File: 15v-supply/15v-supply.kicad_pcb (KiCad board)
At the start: 2 copper layers, 127.5 x 101.9 mm, 0 parts

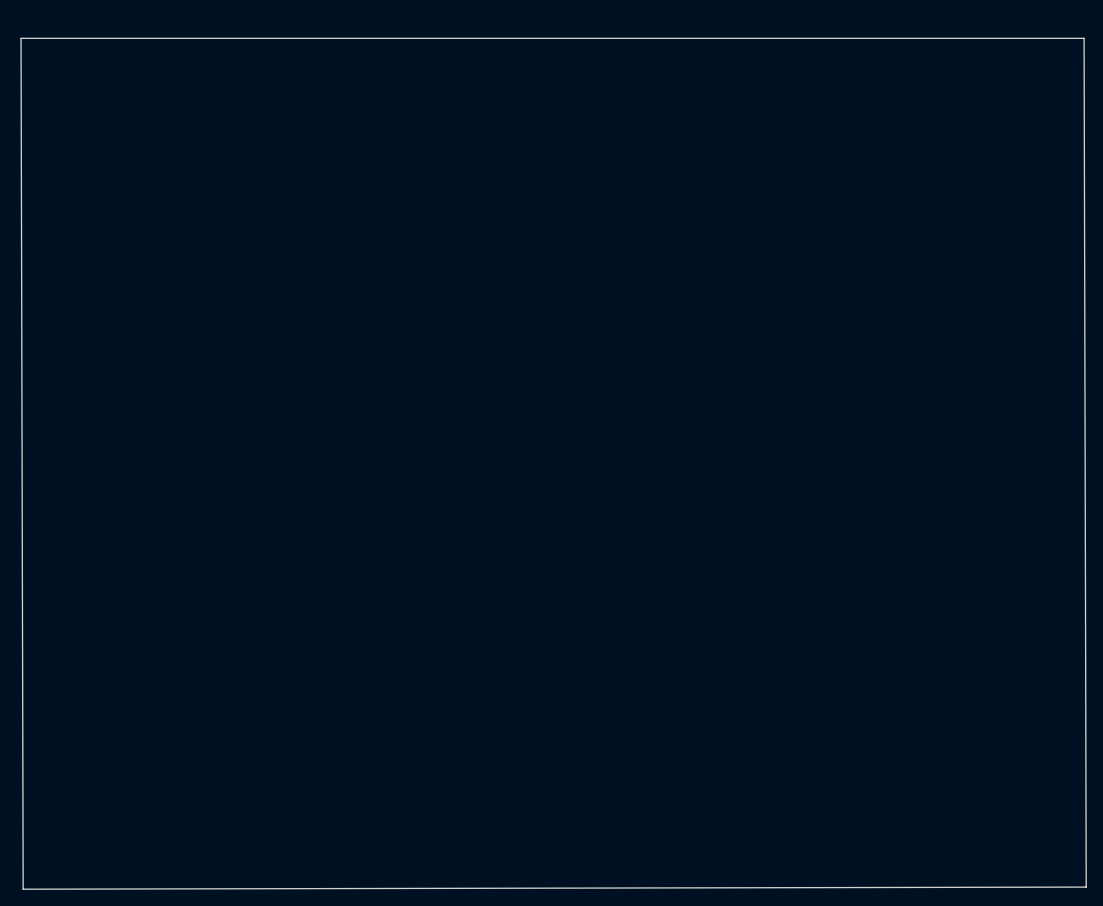
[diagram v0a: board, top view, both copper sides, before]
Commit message: 15v-supply routed and poured
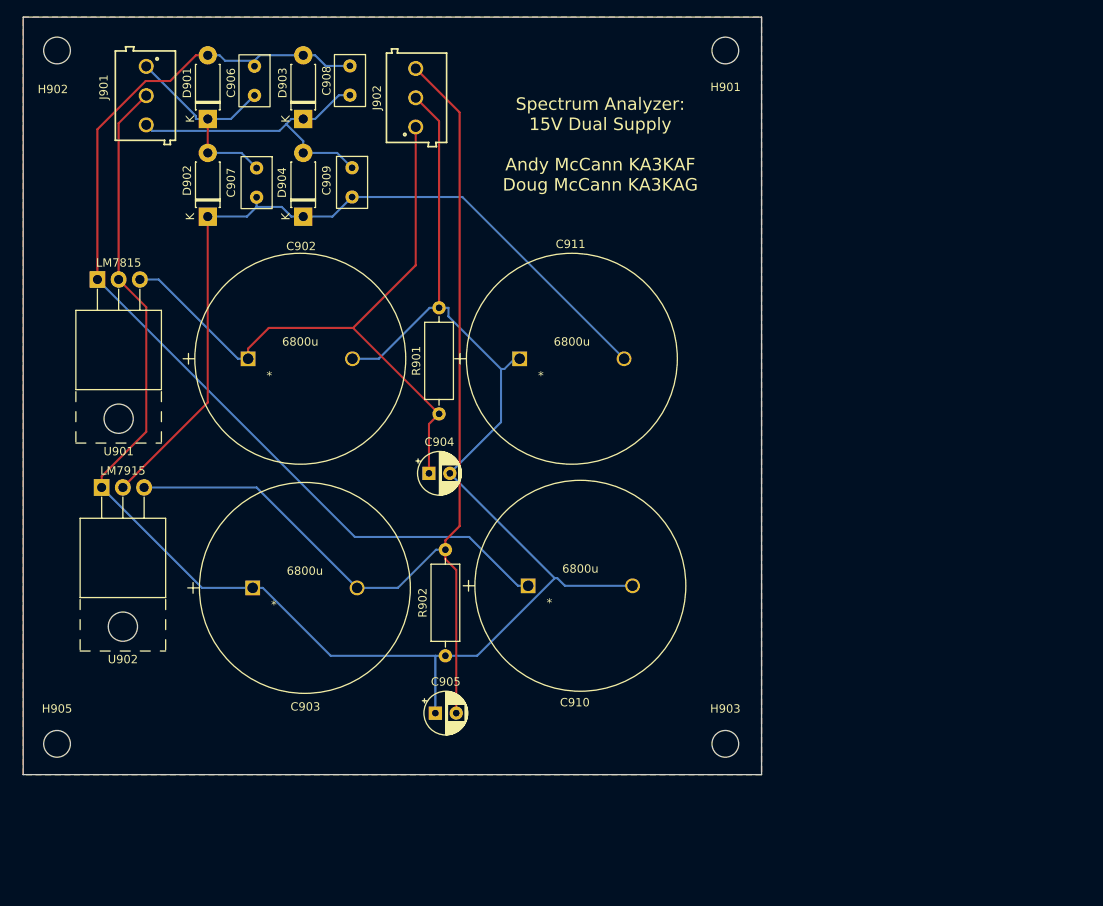
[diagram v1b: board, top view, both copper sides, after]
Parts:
- added C902: 6800u, 15v-supply:6800u-UVR1H682MRD6, F.Cu at (102.9, 88.9)
- added C903: 6800u, 15v-supply:6800u-UVR1H682MRD6, F.Cu at (103.4, 116.3)
- added C904: 6.8u, Capacitor_THT:CP_Radial_D5.0mm_P2.50mm, F.Cu at (124.5, 102.6)
- added C905: 6.8u, Capacitor_THT:CP_Radial_D5.0mm_P2.50mm, F.Cu at (125.3, 131.3)
- added C906: 0.01u, 15v-supply:C_Rect_L6.0mm_W3.5mm_P3.5mm_QYX1H103JTP3TA, F.Cu at (103.6, 53.9)
- added C907: 0.01u, 15v-supply:C_Rect_L6.0mm_W3.5mm_P3.5mm_QYX1H103JTP3TA, F.Cu at (103.9, 66.1)
- added C908: 0.01u, 15v-supply:C_Rect_L6.0mm_W3.5mm_P3.5mm_QYX1H103JTP3TA, F.Cu at (115.1, 53.8)
- added C909: 0.01u, 15v-supply:C_Rect_L6.0mm_W3.5mm_P3.5mm_QYX1H103JTP3TA, F.Cu at (115.3, 66.0)
- added C910: 6800u, 15v-supply:6800u-UVR1H682MRD6, F.Cu at (136.4, 116.1)
- added C911: 6800u, 15v-supply:6800u-UVR1H682MRD6, F.Cu at (135.4, 88.9)
- added D901: 1n5060, Diode_THT:D_DO-41_SOD81_P7.62mm_Horizontal, F.Cu at (98.0, 60.2)
- added D902: 1n5060, Diode_THT:D_DO-41_SOD81_P7.62mm_Horizontal, F.Cu at (98.0, 71.9)
- added D903: 1n5060, Diode_THT:D_DO-41_SOD81_P7.62mm_Horizontal, F.Cu at (109.5, 60.2)
- added D904: 1n5060, Diode_THT:D_DO-41_SOD81_P7.62mm_Horizontal, F.Cu at (109.5, 71.9)
- added H901: MountingHole, MountingHole:MountingHole_3.2mm_M3, F.Cu at (160.0, 52.0)
- added H902: MountingHole, MountingHole:MountingHole_3.2mm_M3, F.Cu at (80.0, 52.0)
- added H903: MountingHole, MountingHole:MountingHole_3.2mm_M3, F.Cu at (160.0, 135.0)
- added H905: MountingHole, MountingHole:MountingHole_3.2mm_M3, F.Cu at (80.0, 135.0)
- added J901: 691103110003, 15v-supply:terminal-block-691103110003, F.Cu at (90.7, 57.4)
- added J902: 691103110003, 15v-supply:terminal-block-691103110003, F.Cu at (122.9, 57.7)
- added R901: 2.2k, Resistor_THT:R_Axial_DIN0309_L9.0mm_D3.2mm_P12.70mm_Horizontal, F.Cu at (125.7, 95.5)
- added R902: 2.2k, Resistor_THT:R_Axial_DIN0309_L9.0mm_D3.2mm_P12.70mm_Horizontal, F.Cu at (126.5, 124.5)
- added U901: LM7815, Package_TO_SOT_THT:TO-220-3_Horizontal_TabUp, F.Cu at (84.8, 79.4)
- added U902: LM7915, Package_TO_SOT_THT:TO-220-3_Horizontal_TabUp, F.Cu at (85.3, 104.3)
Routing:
- net GND: track 0.00 -> 220.6 mm
- net /-15 REGULATED: track 0.00 -> 123.5 mm
- net /7815 IN: track 0.00 -> 120.3 mm
- net /7915 IN: track 0.00 -> 97.6 mm
- net /+15 REGULATED: track 0.00 -> 81.0 mm
- net /TRAN OUT2: track 0.00 -> 37.3 mm
- net /TRAN OUT1: track 0.00 -> 27.6 mm
- added copper zone on B.Cu, net GND
- added copper zone on F.Cu, net GND
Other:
- board size 127.5 x 101.9 mm -> 88.4 x 90.7 mm
- board text added: "Spectrum Analyzer: 15V Dual Supply Andy McCann KA3KAF Doug McCann KA3KAG"

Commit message: if and log amp routing and 3d model
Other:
- board text added: "Spectrum Analyzer: 15V Dual Supply Rev 0.0 Andy McCann KA3KAF Doug McCann KA3KAG"
- board text removed: "Spectrum Analyzer: 15V Dual Supply Andy McCann KA3KAF Doug McCann KA3KAG"
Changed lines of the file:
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@@
   )
   (gr_rect (start 75.946 48.006) (end 164.338 138.684) (layer "Edge.Cuts") (width 0.1) (fill none))
-  (gr_text "Spectrum Analyzer: \n15V Dual Supply\n\nAndy McCann KA3KAF\nDoug McCann KA3KAG" (at 145.034 63.246) (layer "F.SilkS")
-    (effects (font (size 1.5 1.5) (thickness 0.3)))
+  (gr_text "Spectrum Analyzer: \n15V Dual Supply \nRev 0.0\n\nAndy McCann KA3KAF\nDoug McCann KA3KAG" (at 131.826 62.484) (layer "F.SilkS")
+    (effects (font (size 1.5 1.5) (thickness 0.3)) (justify left))
   )
   (segment (start 124.5249 96.7091) (end 125.73 95.504) (width 0.25) (layer "F.Cu") (net 1))

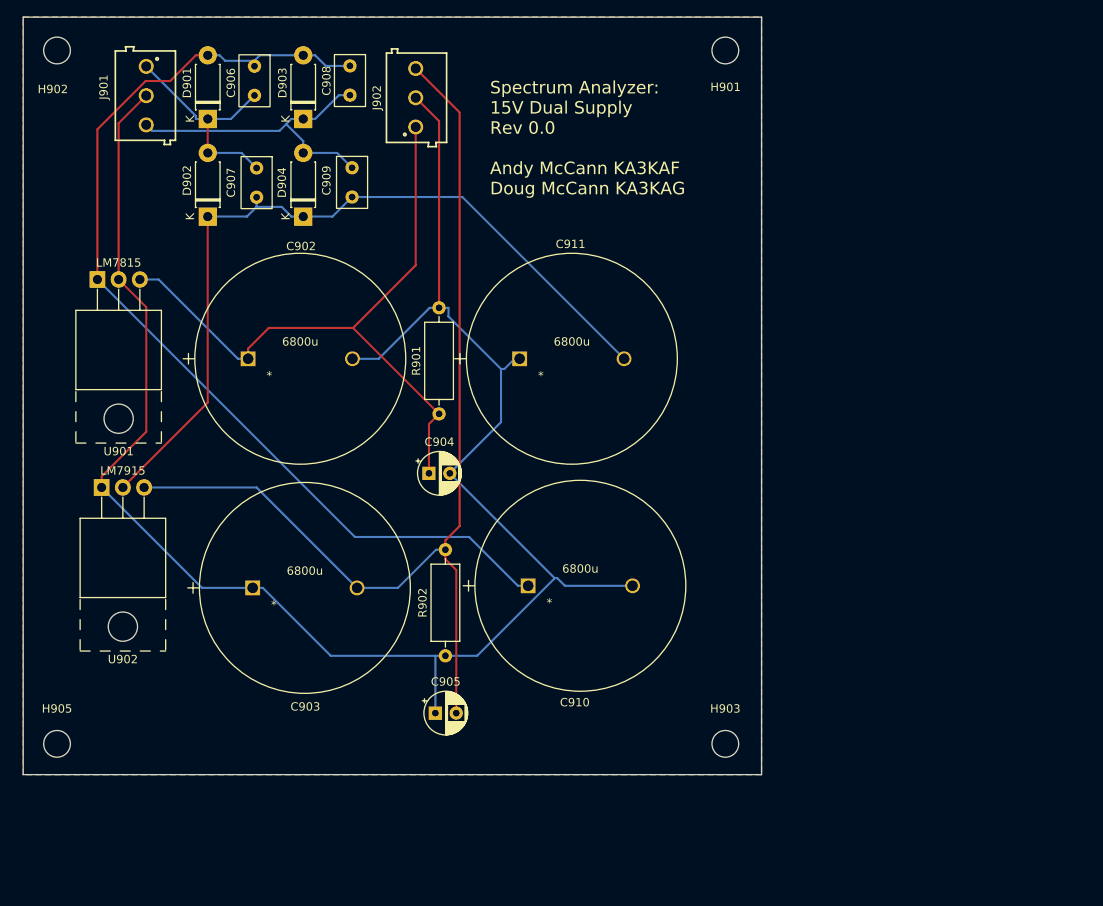
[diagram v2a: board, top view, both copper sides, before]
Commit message: updates to 15v supply and if and log amp boards so boards can be sent to fab
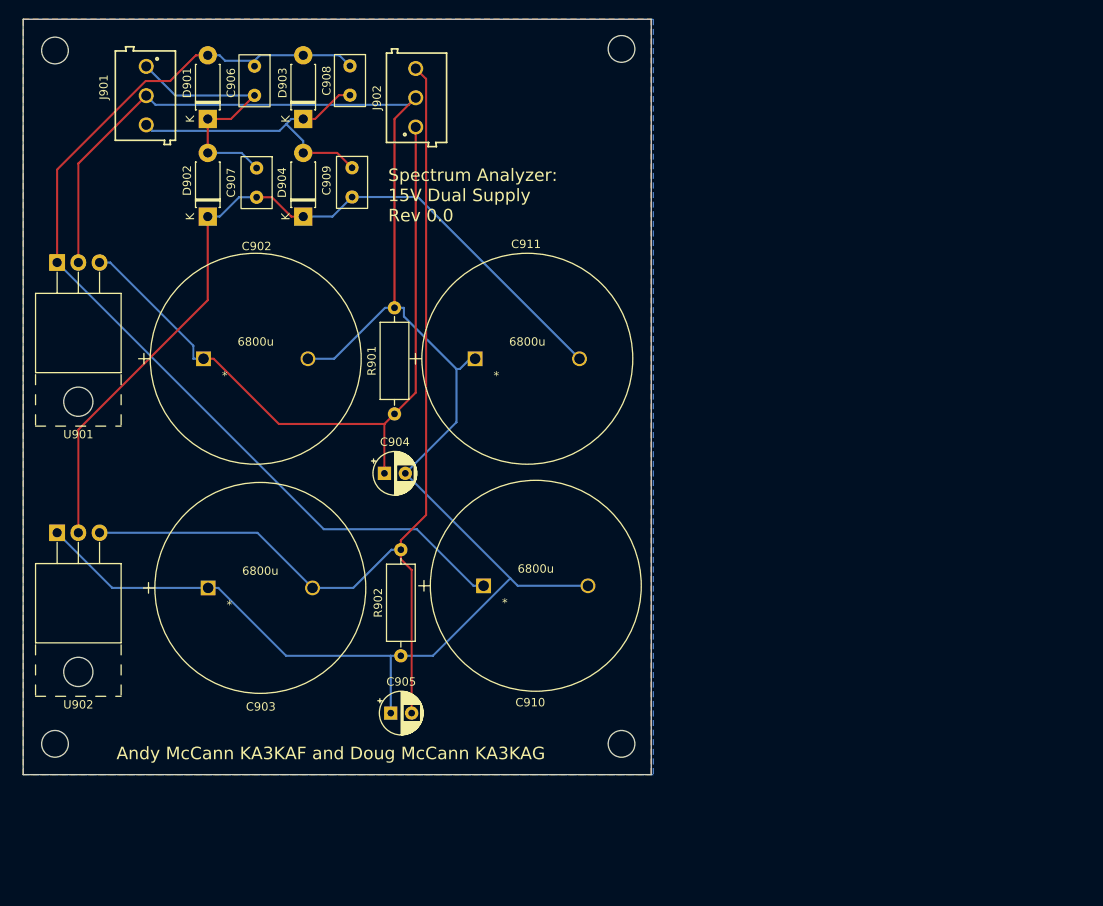
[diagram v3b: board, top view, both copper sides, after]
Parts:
- moved H901 12.4 mm to (147.6, 51.8)
- moved H903 12.4 mm to (147.6, 135.0)
- moved U902 7.60 mm to (80.0, 109.7)
- moved C902 5.33 mm to (97.5, 88.9)
- moved C904 5.33 mm to (119.2, 102.6)
- moved C905 5.33 mm to (120.0, 131.3)
- moved C910 5.33 mm to (131.1, 116.1)
- moved C911 5.33 mm to (130.0, 88.9)
- moved R901 5.33 mm to (120.4, 95.5)
- moved R902 5.33 mm to (121.2, 124.5)
- moved C903 5.33 mm to (98.1, 116.3)
- moved U901 5.24 mm to (80.0, 77.4)
- moved H902 0.24 mm to (79.8, 52.0)
- moved H905 0.24 mm to (79.8, 135.0)
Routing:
- net /+15 REGULATED: track 81.0 -> 86.0 mm
- net /TRAN OUT1: track 27.6 -> 31.8 mm
- net /-15 REGULATED: track 123.5 -> 120.2 mm
- net GND: track 220.6 -> 222.8 mm
- net /7915 IN: track 97.6 -> 99.7 mm
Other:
- board size 88.4 x 90.7 mm -> 75.2 x 90.4 mm
- board text added: "Andy McCann KA3KAF and Doug McCann KA3KAG"
- board text added: "Spectrum Analyzer: 15V Dual Supply Rev 0.0"
- board text removed: "Spectrum Analyzer: 15V Dual Supply Rev 0.0 Andy McCann KA3KAF Doug McCann KA3KAG"

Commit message: 15v-supply changes
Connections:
- D901 pad 1: /TRAN OUT1 -> /7815 IN
- D901 pad 2: /7815 IN -> /TRAN OUT1
- D902 pad 1: /7915 IN -> /TRAN OUT2
- D902 pad 2: /TRAN OUT1 -> /7915 IN
- D903 pad 1: /TRAN OUT2 -> /7815 IN
- D903 pad 2: /7815 IN -> /TRAN OUT2
- D904 pad 1: /7915 IN -> /TRAN OUT2
- D904 pad 2: /TRAN OUT2 -> /7915 IN
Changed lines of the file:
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@@
     (property "Spice_Model" "1N5060")
     (property "Spice_Netlist_Enabled" "Y")
+    (property "Spice_Node_Sequence" "2 1")
     (property "Spice_Primitive" "D")
     (attr through_hole)
@@
     (fp_line (start 7.62 0) (end 6.41 0) (layer "F.Fab") (width 0.1))
     (pad "1" thru_hole rect (at 0 0 90) (size 2.2 2.2) (drill 1.1) (layers *.Cu *.Mask)
-      (net 5 "/TRAN OUT1") (pinfunction "Cathode") (pintype "passive"))
+      (net 4 "/7815 IN") (pinfunction "Cathode") (pintype "passive"))
     (pad "2" thru_hole oval (at 7.62 0 90) (size 2.2 2.2) (drill 1.1) (layers *.Cu *.Mask)
-      (net 4 "/7815 IN") (pinfunction "Anode") (pintype "passive"))
+      (net 5 "/TRAN OUT1") (pinfunction "Anode") (pintype "passive"))
     (model "${KICAD6_3DMODEL_DIR}/Diode_THT.3dshapes/D_DO-41_SOD81_P7.62mm_Horizontal.wrl"
       (offset (xyz 0 0 0))
@@
     (property "Spice_Model" "1N5060")
     (property "Spice_Netlist_Enabled" "Y")
+    (property "Spice_Node_Sequence" "2 1")
     (property "Spice_Primitive" "D")
     (attr through_hole)
@@
     (fp_line (start 1.99 -1.35) (end 1.99 1.35) (layer "F.Fab") (width 0.1))
     (pad "1" thru_hole rect (at 0 0 90) (size 2.2 2.2) (drill 1.1) (layers *.Cu *.Mask)
-      (net 6 "/7915 IN") (pinfunction "Cathode") (pintype "passive"))
+      (net 7 "/TRAN OUT2") (pinfunction "Cathode") (pintype "passive"))
     (pad "2" thru_hole oval (at 7.62 0 90) (size 2.2 2.2) (drill 1.1) (layers *.Cu *.Mask)
-      (net 7 "/TRAN OUT2") (pinfunction "Anode") (pintype "passive"))
+      (net 6 "/7915 IN") (pinfunction "Anode") (pintype "passive"))
     (model "${KICAD6_3DMODEL_DIR}/Diode_THT.3dshapes/D_DO-41_SOD81_P7.62mm_Horizontal.wrl"
       (offset (xyz 0 0 0))
@@
     (property "Spice_Model" "1N5060")
     (property "Spice_Netlist_Enabled" "Y")
+    (property "Spice_Node_Sequence" "2 1")
     (property "Spice_Primitive" "D")
     (attr through_hole)
@@
     (fp_line (start 1.21 -1.35) (end 1.21 1.35) (layer "F.Fab") (width 0.1))
     (pad "1" thru_hole rect (at 0 0 90) (size 2.2 2.2) (drill 1.1) (layers *.Cu *.Mask)
-      (net 6 "/7915 IN") (pinfunction "Cathode") (pintype "passive"))
+      (net 7 "/TRAN OUT2") (pinfunction "Cathode") (pintype "passive"))
     (pad "2" thru_hole oval (at 7.62 0 90) (size 2.2 2.2) (drill 1.1) (layers *.Cu *.Mask)
-      (net 5 "/TRAN OUT1") (pinfunction "Anode") (pintype "passive"))
+      (net 6 "/7915 IN") (pinfunction "Anode") (pintype "passive"))
     (model "${KICAD6_3DMODEL_DIR}/Diode_THT.3dshapes/D_DO-41_SOD81_P7.62mm_Horizontal.wrl"
       (offset (xyz 0 0 0))
@@
     (property "Spice_Model" "1N5060")
     (property "Spice_Netlist_Enabled" "Y")
+    (property "Spice_Node_Sequence" "2 1")
     (property "Spice_Primitive" "D")
     (attr through_hole)
@@
     (fp_line (start 1.89 -1.35) (end 1.89 1.35) (layer "F.Fab") (width 0.1))
     (pad "1" thru_hole rect (at 0 0 90) (size 2.2 2.2) (drill 1.1) (layers *.Cu *.Mask)
-      (net 7 "/TRAN OUT2") (pinfunction "Cathode") (pintype "passive"))
+      (net 4 "/7815 IN") (pinfunction "Cathode") (pintype "passive"))
     (pad "2" thru_hole oval (at 7.62 0 90) (size 2.2 2.2) (drill 1.1) (layers *.Cu *.Mask)
-      (net 4 "/7815 IN") (pinfunction "Anode") (pintype "passive"))
+      (net 7 "/TRAN OUT2") (pinfunction "Anode") (pintype "passive"))
     (model "${KICAD6_3DMODEL_DIR}/Diode_THT.3dshapes/D_DO-41_SOD81_P7.62mm_Horizontal.wrl"
       (offset (xyz 0 0 0))

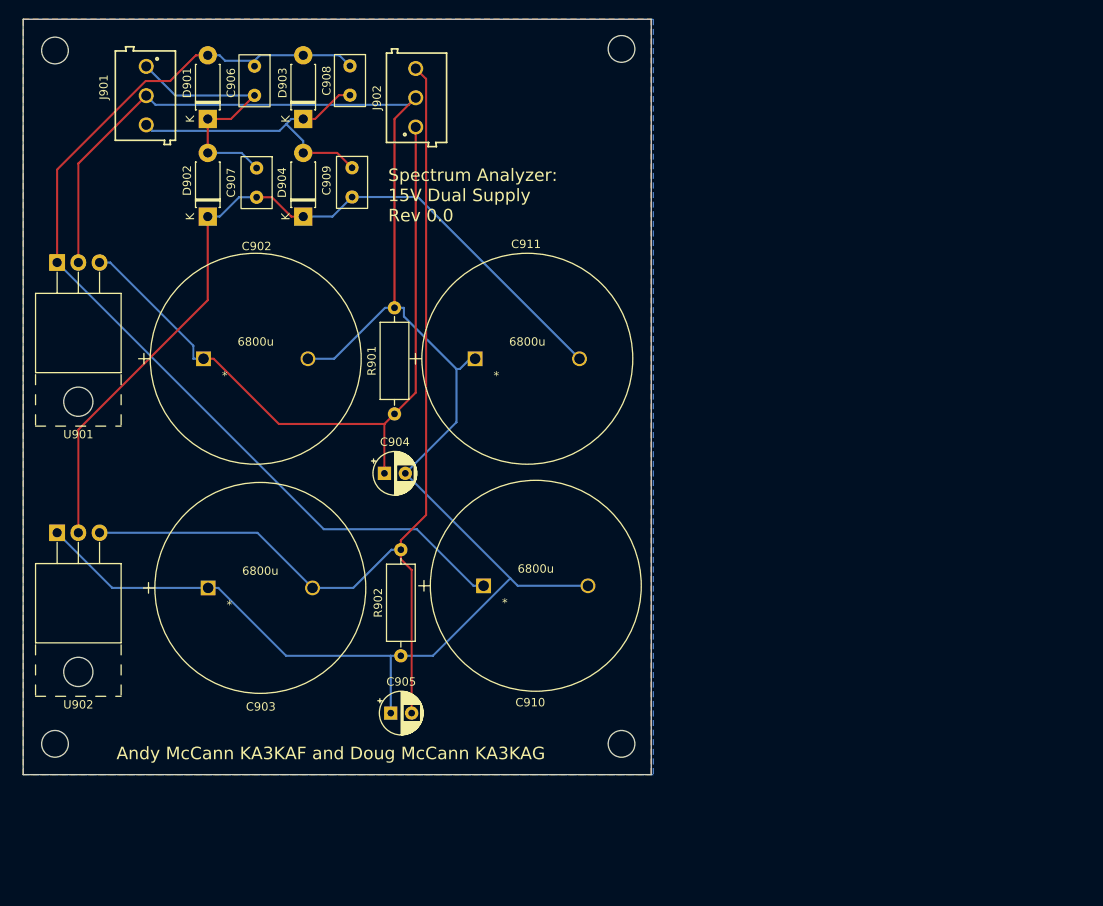
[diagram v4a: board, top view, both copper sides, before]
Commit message: 15v-supply updates
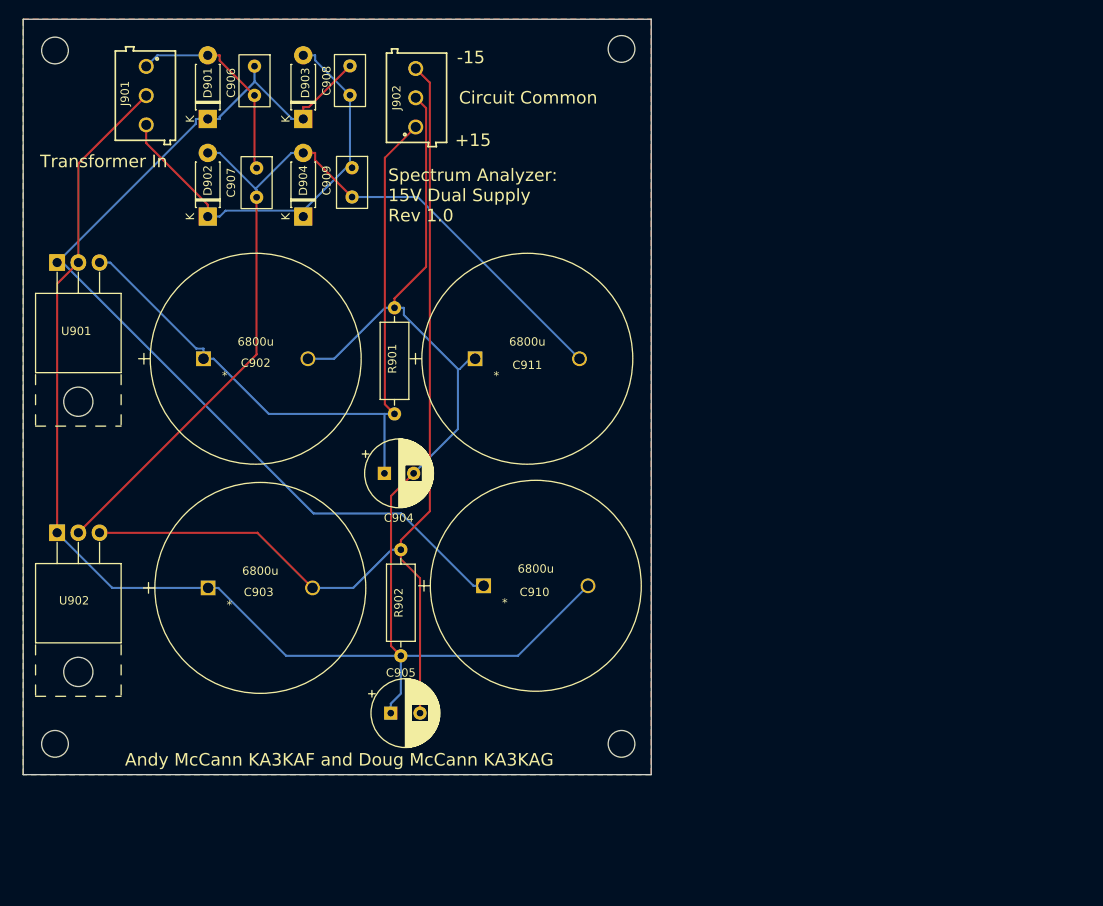
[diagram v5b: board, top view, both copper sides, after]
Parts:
- C904, C905: footprint Capacitor_THT:CP_Radial_D5.0mm_P2.50mm -> Capacitor_THT:CP_Radial_D8.0mm_P3.50mm
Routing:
- net /TRAN OUT2: track 37.3 -> 51.0 mm
- net /7915 IN: track 99.7 -> 108.8 mm
- net /TRAN OUT1: track 31.8 -> 24.7 mm
- net GND: track 222.8 -> 229.2 mm
- net /7815 IN: track 120.6 -> 118.6 mm
- net /+15 REGULATED: track 86.0 -> 87.0 mm
- net /-15 REGULATED: track 120.2 -> 120.9 mm
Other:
- board text added: "+15"
- board text added: "-15"
- board text added: "Circuit Common"
- board text added: "Spectrum Analyzer: 15V Dual Supply Rev 1.0"
- board text added: "Transformer In"
- board text removed: "Spectrum Analyzer: 15V Dual Supply Rev 0.0"
